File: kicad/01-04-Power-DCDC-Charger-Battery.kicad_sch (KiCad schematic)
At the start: 43 parts, among them J3 S2B-PH-K-S_LF__SN_, Q1 PMOS, Q2 AO3400A, Q3 AO3400A, U2 BQ29700DSER, U3 MCP73831-2-OT, U4 TLV62568DBV

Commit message: added 32.768 oscillator
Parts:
- U3: MPN (none) -> ABS06-32.768KHZ-9-T; Manufacturer (none) -> Abracon LLC; Package (none) -> SMD2012-2P; Supplier 1 (none) -> LSCS; Supplier 1 SKU (none) -> C1985410; Supplier 1 URL (none) -> https://lcsc.com/product-detail/crystals_abracon-llc-abs06-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
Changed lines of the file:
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@@
+			)
+		)
+		(property "MPN" "ABS06-32.768KHZ-9-T"
+			(at 146.05 39.37 0)
+			(effects
+				(font
+					(size 1.27 1.27)
+				)
+				(hide yes)
+			)
+		)
+		(property "Manufacturer" "Abracon LLC"
+			(at 146.05 39.37 0)
+			(effects
+				(font
+					(size 1.27 1.27)
+				)
+				(hide yes)
+			)
+		)
+		(property "Package" "SMD2012-2P"
+			(at 146.05 39.37 0)
+			(effects
+				(font
+					(size 1.27 1.27)
+				)
+				(hide yes)
+			)
+		)
+		(property "Supplier 1" "LSCS"
+			(at 146.05 39.37 0)
+			(effects
+				(font
+					(size 1.27 1.27)
+				)
+				(hide yes)
+			)
+		)
+		(property "Supplier 1 SKU" "C1985410"
+			(at 146.05 39.37 0)
+			(effects
+				(font
+					(size 1.27 1.27)
+				)
+				(hide yes)
+			)
+		)
+		(property "Supplier 1 URL" "https://lcsc.com/product-detail/crystals_abracon-llc-abs06-32-768khz-9-t_C1985410.html"
+			(at 146.05 39.37 0)
+			(effects
+				(font
+					(size 1.27 1.27)
+				)
+				(hide yes)
 			)
 		)

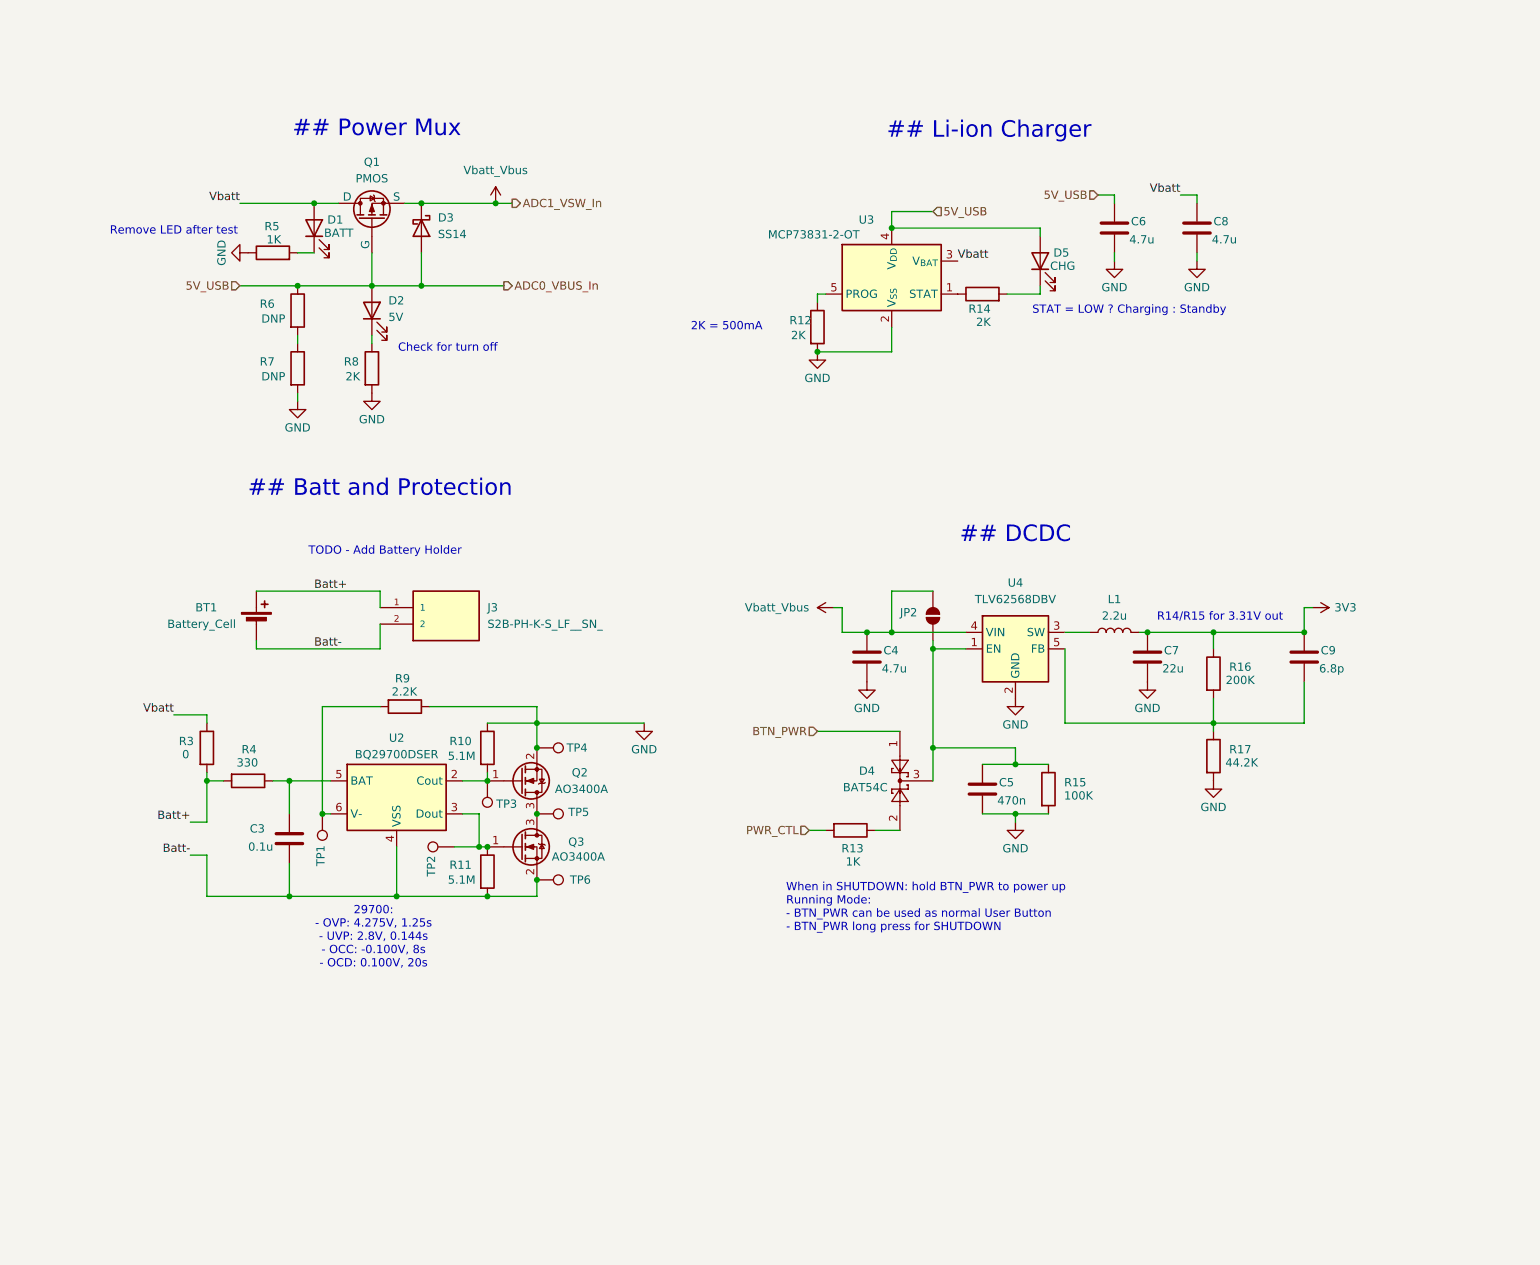
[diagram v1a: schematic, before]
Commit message: low speed xtal added
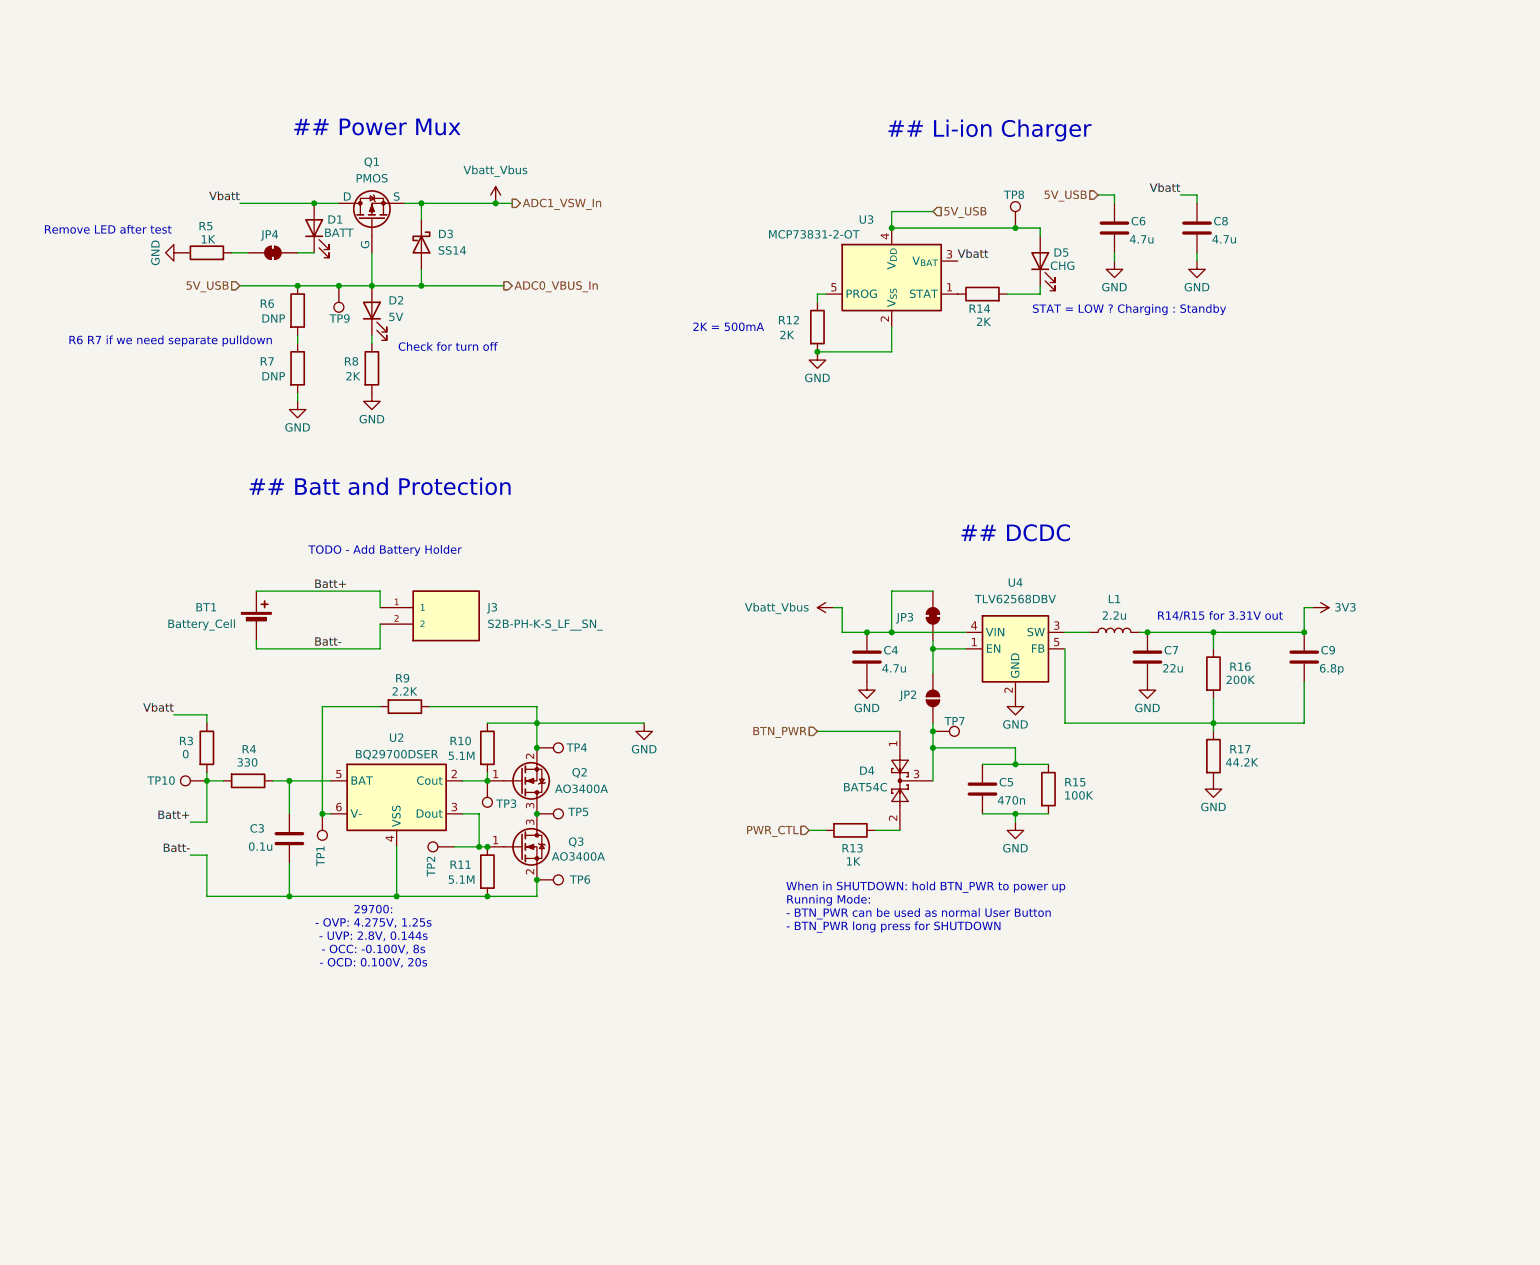
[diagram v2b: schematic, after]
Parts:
- added JP3, JP4: SolderJumper_2_Bridged, symbol Jumper:SolderJumper_2_Bridged
- added TP10, TP7, TP8, TP9: TestPoint, symbol Connector:TestPoint
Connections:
- net 5V_USB: now also TP8.1, TP9.1
- net Batt+: now also TP10.1
- net Vbatt_Vbus: now also JP3.2 (B); no longer JP2.2 (B)
- net at C5.1, D4.3, JP2.1 (A)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: now also TP7.1; no longer U4.1 (EN)
- net at D1.1 (K): now also JP4.1 (A); no longer R5.2
- new net: JP2.2 (B), JP3.1 (A), U4.1 (EN)
- new net: JP4.2 (B), R5.2
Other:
- note added: "R6 R7 if we need separate pulldown"
- moved on the sheet: D3, JP2, R5

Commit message: rtc hardware
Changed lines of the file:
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@@
+	)
+	(junction
+		(at 38.1 106.68)
+		(diameter 0)
+		(color 0 0 0 0)
 	)
 	(junction
@@
 	(wire
 		(pts
+			(xy 34.29 104.14) (xy 38.1 104.14)
+		)
+		(stroke
+			(width 0)
+			(type default)
+		)
+	)
+	(wire
+		(pts
 			(xy 44.45 35.56) (xy 46.99 35.56)
 		)
@@
 	(wire
 		(pts
-			(xy 35.56 106.68) (xy 40.64 106.68)
+			(xy 35.56 106.68) (xy 38.1 106.68)
 		)
 		(stroke
@@
 	(wire
 		(pts
+			(xy 38.1 106.68) (xy 40.64 106.68)
+		)
+		(stroke
+			(width 0)
+			(type default)
+		)
+	)
+	(wire
+		(pts
 			(xy 66.04 40.64) (xy 73.66 40.64)
 		)
@@
 		(pts
 			(xy 146.05 46.99) (xy 146.05 50.8)
+		)
+		(stroke
+			(width 0)
+			(type default)
+		)
+	)
+	(wire
+		(pts
+			(xy 38.1 104.14) (xy 38.1 106.68)
 		)
 		(stroke
@@
 		)
 	)
+	(label "Vbatt"
+		(at 34.29 104.14 180)
+		(effects
+			(font
+				(size 1.27 1.27)
+			)
+			(justify right bottom)
+		)
+	)
 	(label "Batt+"
 		(at 57.15 87.63 0)
@@
 	(label "Batt-"
 		(at 38.1 128.27 180)
-		(effects
-			(font
-				(size 1.27 1.27)
-			)
-			(justify right bottom)
-		)
-	)
-	(label "Vbatt"
-		(at 35.56 106.68 180)
 		(effects
 			(font
@@
 		)
 	)
-	(hierarchical_label "ADC0_VBUS_In"
+	(hierarchical_label "ADC0_VUSB_In"
 		(shape output)
 		(at 86.36 40.64 0)
@@
 		(effects
 			(font
+				(size 1.27 1.27)
+			)
+			(justify right)
+		)
+	)
+	(hierarchical_label "Vbatt"
+		(shape output)
+		(at 35.56 106.68 180)
+		(effects
+			(font
